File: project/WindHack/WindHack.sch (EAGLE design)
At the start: 48 parts, among them SW1 SSSS810701, SW2 SSSS810701, U1 LazuriteBLE, U10 BK-913, U2 BM1383AGLV, U3 KXG03, U4 BM1422AGMV, U5 DF40C-20DS-0.4V, U6 BHXXPB1WFV, U7 MOLEX-SD-503398-1892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

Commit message: modified to rev1A
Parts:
- removed D2: RF071MM2S, lz-shield:RF071MM2S
- removed R10: 100, rcl:R-EU_R0603
- removed R15: 0, rcl:R-EU_R0603
- C6: value 0.1uF -> 1uF
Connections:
- net ACCEL_INT renamed GYRO_INT
- net BT_SW renamed RF_SW
- removed net +2.4V_RSV: R10.2, U10.VDD1, U10.VDD2
- removed net GPS_PRS: R15.2, U1C.7
- removed net N$9: D2.C, R10.1
- new net +3V_RSV: C6.1, D1.A, U5.14
- net +3V3: no longer C6.1, D1.A, U5.14
- net GND: no longer R15.1
- net N$8: now also U10.VDD1, U10.VDD2; no longer D2.A
- net TEST0: now also U$1.7_1; no longer U$1.7_2
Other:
- note added: "Yoshiyuki Tanaka"
- note removed: "2.4V"
- moved on the sheet: C14, C3, C4, C5, C6, D1, R9, U10, U3, U5

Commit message: updated to rev 1A'
- moved C6/C4/D1 location
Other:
- note added: "Rev1A'"
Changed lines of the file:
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@@
 <part name="GND25" library="supply1" deviceset="GND" device=""/>
 <part name="+3V10" library="supply1" deviceset="+3V3" device=""/>
-<part name="GND27" library="supply1" deviceset="GND" device=""/>
 <part name="U8" library="con-hirose" deviceset="MICRO-USB-SHIELD-" device="ZX62R-B-5P"/>
 <part name="GND28" library="supply1" deviceset="GND" device=""/>
@@
 <text x="172.72" y="15.24" size="3.81" layer="95">BT SW</text>
 <text x="294.64" y="12.7" size="3.81" layer="95">Yoshiyuki Tanaka</text>
+<text x="343.916" y="20.32" size="2.54" layer="95">Rev1A'</text>
 </plain>
 <instances>
@@
 <instance part="GND25" gate="1" x="182.88" y="96.52"/>
 <instance part="+3V10" gate="G$1" x="96.52" y="71.12"/>
-<instance part="GND27" gate="1" x="200.66" y="101.6"/>
 <instance part="U8" gate="G$1" x="246.38" y="213.36" smashed="yes" rot="MR0">
 <attribute name="NAME" x="242.57" y="215.9" size="1.778" layer="95" font="vector" rot="MR0"/>
@@
 <pinref part="U5" gate="G$1" pin="12"/>
 <wire x1="205.74" y1="129.54" x2="203.2" y2="129.54" width="0.1524" layer="91"/>
-<wire x1="203.2" y1="129.54" x2="203.2" y2="109.22" width="0.1524" layer="91"/>
+<wire x1="203.2" y1="129.54" x2="203.2" y2="119.38" width="0.1524" layer="91"/>
+<wire x1="203.2" y1="119.38" x2="203.2" y2="109.22" width="0.1524" layer="91"/>
 <wire x1="203.2" y1="109.22" x2="233.68" y2="109.22" width="0.1524" layer="91"/>
 <junction x="233.68" y="109.22"/>
 <junction x="203.2" y="129.54"/>
+<pinref part="U5" gate="G$1" pin="20"/>
+<wire x1="205.74" y1="119.38" x2="203.2" y2="119.38" width="0.1524" layer="91"/>
+<junction x="203.2" y="119.38"/>
 </segment>
 <segment>
@@
 <wire x1="190.5" y1="106.68" x2="182.88" y2="106.68" width="0.1524" layer="91"/>
 <junction x="182.88" y="106.68"/>
-</segment>
-<segment>
-<pinref part="U5" gate="G$1" pin="20"/>
-<wire x1="205.74" y1="119.38" x2="200.66" y2="119.38" width="0.1524" layer="91"/>
-<wire x1="200.66" y1="119.38" x2="200.66" y2="104.14" width="0.1524" layer="91"/>
-<pinref part="GND27" gate="1" pin="GND"/>
 </segment>
 <segment>
@@
 </sheet>
 </sheets>
+<errors>
+</errors>
 </schematic>
 </drawing>

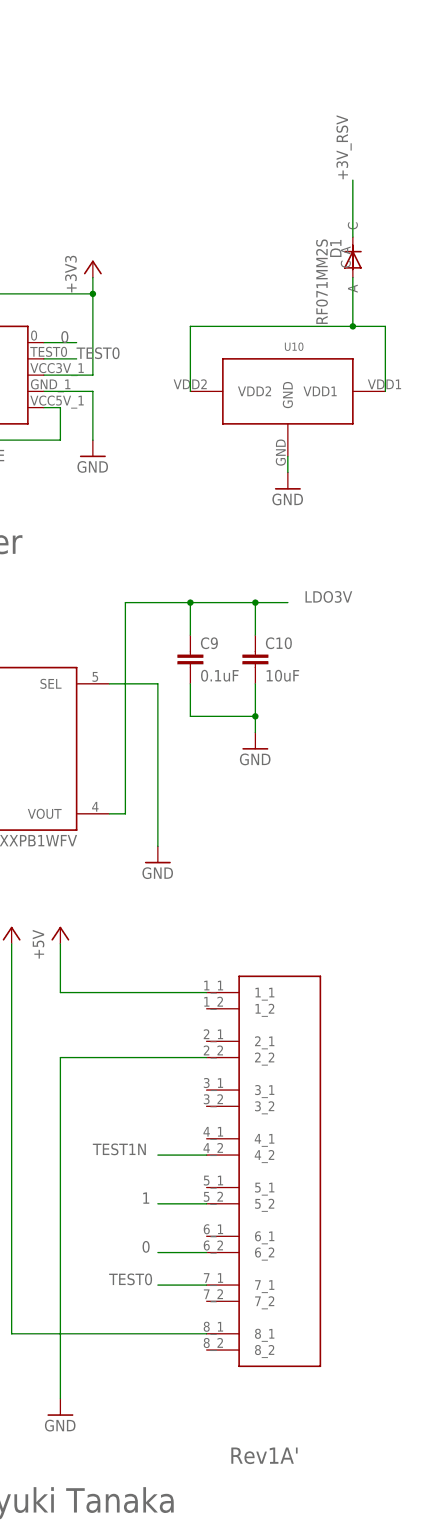
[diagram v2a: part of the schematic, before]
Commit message: update WindHack and lz-shield(RF071MM2S)
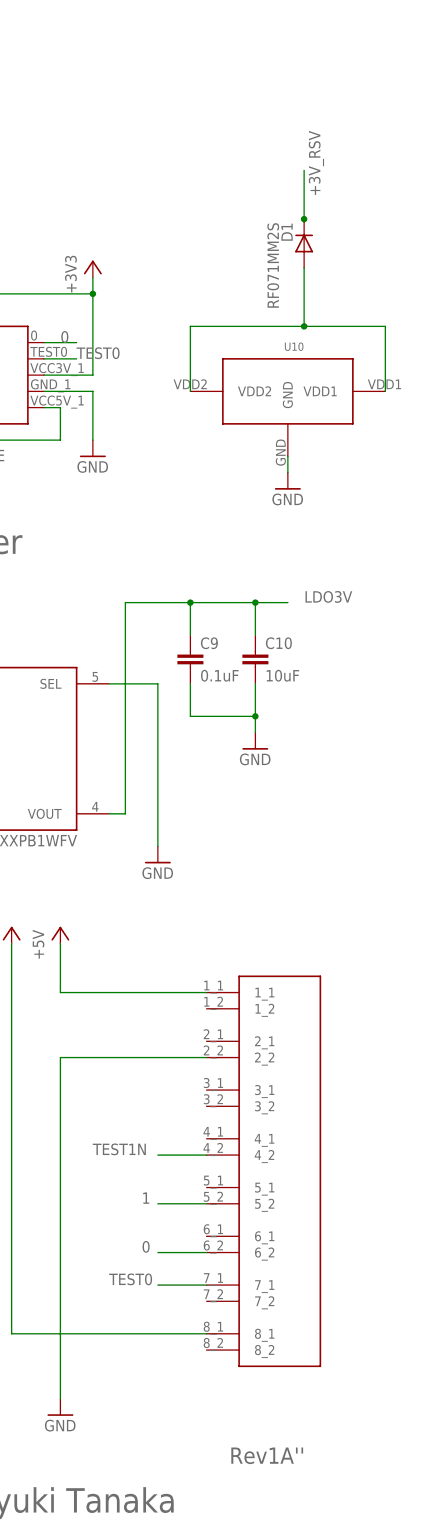
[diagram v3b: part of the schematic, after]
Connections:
- net +3V_RSV: now also D1.C; no longer D1.A
- net N$8: now also D1.A; no longer D1.C
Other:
- note added: "Rev1A''"
- note removed: "Rev1A'"
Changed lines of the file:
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@@
 <text x="172.72" y="15.24" size="3.81" layer="95">BT SW</text>
 <text x="294.64" y="12.7" size="3.81" layer="95">Yoshiyuki Tanaka</text>
-<text x="343.916" y="20.32" size="2.54" layer="95">Rev1A'</text>
+<text x="343.916" y="20.32" size="2.54" layer="95">Rev1A''</text>
 </plain>
 <instances>
@@
 <attribute name="VALUE" x="259.08" y="175.26" size="1.778" layer="96"/>
 </instance>
-<instance part="D1" gate="G$1" x="363.22" y="208.28" rot="R180"/>
+<instance part="D1" gate="G$1" x="355.6" y="210.82" rot="R180"/>
 <instance part="+3V6" gate="G$1" x="322.58" y="208.28"/>
 <instance part="U4" gate="BM1422AGMV" x="53.34" y="88.9" rot="R180"/>
@@
 <net name="+3V_RSV" class="0">
 <segment>
-<pinref part="D1" gate="G$1" pin="A"/>
-<wire x1="363.22" y1="212.09" x2="363.22" y2="220.98" width="0.1524" layer="91"/>
-<label x="360.68" y="231.14" size="1.778" layer="95" rot="R270"/>
-</segment>
-<segment>
 <pinref part="U5" gate="G$1" pin="14"/>
 <wire x1="205.74" y1="127" x2="190.5" y2="127" width="0.1524" layer="91"/>
@@
 <label x="190.5" y="152.4" size="1.778" layer="95" rot="R90"/>
 </segment>
+<segment>
+<wire x1="355.6" y1="214.884" x2="355.6" y2="222.504" width="0.1524" layer="91"/>
+<label x="358.14" y="218.44" size="1.778" layer="95" rot="R90"/>
+<pinref part="D1" gate="G$1" pin="C"/>
+<junction x="355.6" y="214.884"/>
+</segment>
 </net>
 <net name="RF_SW" class="0">
@@
 <pinref part="U10" gate="G$1" pin="VDD2"/>
 <wire x1="337.82" y1="187.96" x2="337.82" y2="198.12" width="0.1524" layer="91"/>
-<wire x1="337.82" y1="198.12" x2="363.22" y2="198.12" width="0.1524" layer="91"/>
+<wire x1="337.82" y1="198.12" x2="355.6" y2="198.12" width="0.1524" layer="91"/>
 <pinref part="U10" gate="G$1" pin="VDD1"/>
-<wire x1="363.22" y1="198.12" x2="368.3" y2="198.12" width="0.1524" layer="91"/>
+<wire x1="355.6" y1="198.12" x2="368.3" y2="198.12" width="0.1524" layer="91"/>
 <wire x1="368.3" y1="198.12" x2="368.3" y2="187.96" width="0.1524" layer="91"/>
-<pinref part="D1" gate="G$1" pin="C"/>
-<wire x1="363.22" y1="205.74" x2="363.22" y2="198.12" width="0.1524" layer="91"/>
-<junction x="363.22" y="198.12"/>
-</segment>
-</net>
+<pinref part="D1" gate="G$1" pin="A"/>
+<wire x1="355.6" y1="198.12" x2="355.6" y2="207.264" width="0.1524" layer="91"/>
+<junction x="355.6" y="198.12"/>
+</segment>
+</net>
